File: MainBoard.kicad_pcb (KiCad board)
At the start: 2 copper layers, 120 x 68 mm, 89 parts, among them J1 DB25, P1 BOOT, P10 CONN_01X03, P11 CONN_01X03, P12 CONN_01X03, P13 CONN_01X03, P14 CONN_01X02, P15 CONN_02X07, P16 CONN_02X04, P18 CONN_01X03, P2 CONN_01X04, P3 CONN_02X04, P4 HOLE, P5 HOLE, P6 HOLE, P7 HOLE, P8 CONN_01X02, P9 CONN_01X03, Q1 BSS138, Q2 BSS138, Q3 DMN65D8L, SW1 RESET, U1 mp2307, U10 SI4425DDY, U11 INA199A2, U12 ADS1015, U2 DYS_mini_ESC, U3 DYS_mini_ESC, U4 DYS_mini_ESC, U5 DYS_mini_ESC, U6 TLV1117LV33, U7 TENDA_P200, U8 pca9685, U9 STM32F103CBT6, Y1 8MHz

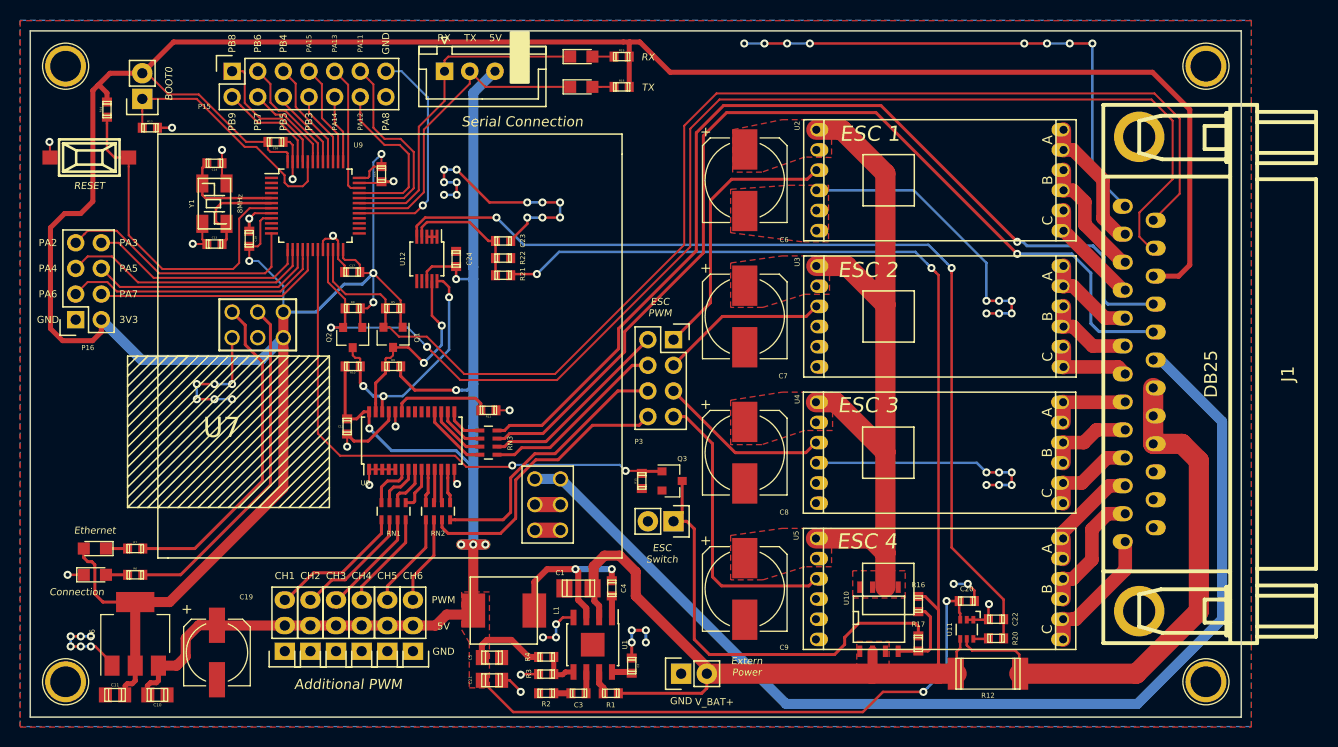
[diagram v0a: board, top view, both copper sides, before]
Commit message: replace groud via
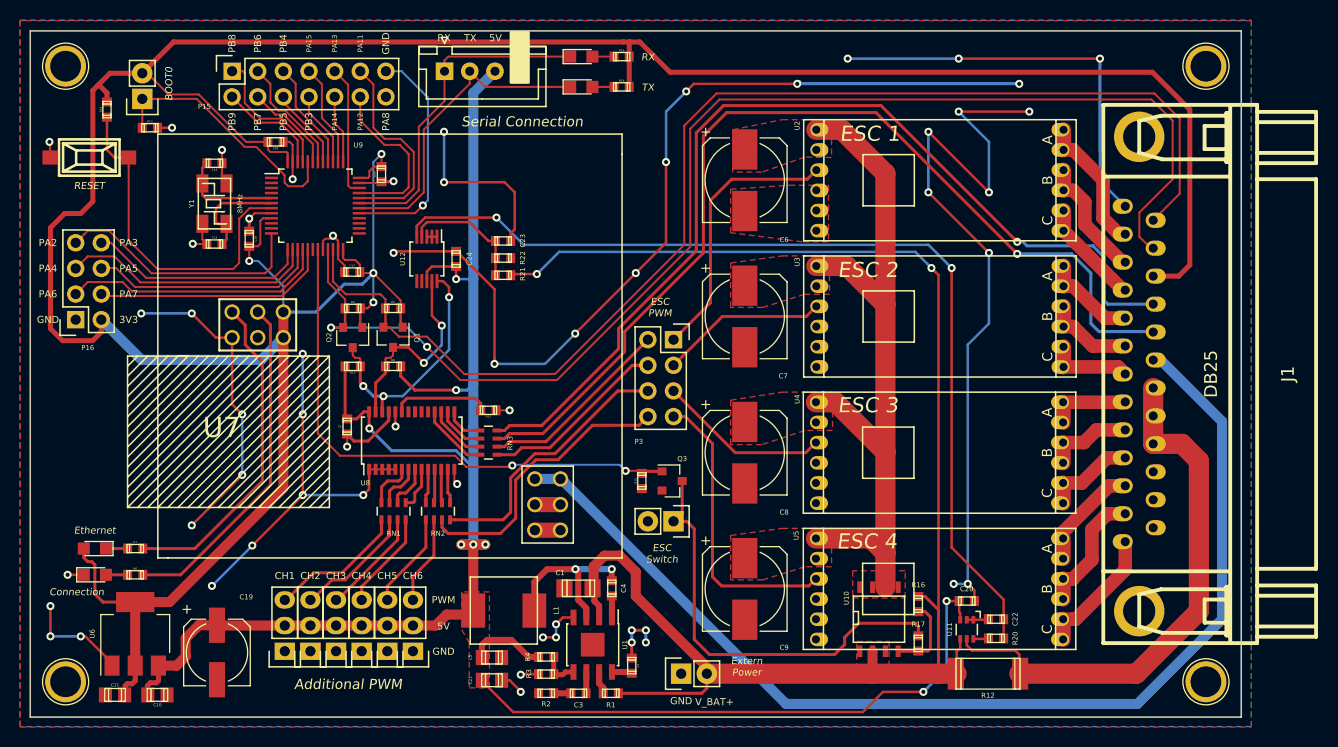
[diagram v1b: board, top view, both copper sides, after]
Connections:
- P4 pad 1: Net-(P4-Pad1) -> (no net)
- P5 pad 1: Net-(P5-Pad1) -> (no net)
- P6 pad 1: Net-(P6-Pad1) -> (no net)
- P7 pad 1: Net-(P7-Pad1) -> (no net)
- U12 pad 6: Net-(U12-Pad6) -> (no net)
- U12 pad 7: Net-(U12-Pad7) -> (no net)
- U7 pad P: Net-(U7-PadP) -> (no net)
- U8 pad 19: Net-(U8-Pad19) -> (no net)
- U8 pad 20: Net-(U8-Pad20) -> (no net)
- U8 pad 21: Net-(U8-Pad21) -> (no net)
- U8 pad 22: Net-(U8-Pad22) -> (no net)
- U9 pad 1: Net-(U9-Pad1) -> (no net)
- U9 pad 10: /PA0 -> (no net)
- U9 pad 11: /PA1 -> (no net)
- U9 pad 18: Net-(U9-Pad18) -> (no net)
- U9 pad 2: Net-(U9-Pad2) -> (no net)
- U9 pad 25: /PB12 -> (no net)
- U9 pad 26: /PB13 -> (no net)
- U9 pad 27: /PB14 -> (no net)
- U9 pad 28: /PB15 -> (no net)
- U9 pad 3: Net-(U9-Pad3) -> (no net)
- U9 pad 4: Net-(U9-Pad4) -> (no net)
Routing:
- net GND: track 227.5 -> 401.5 mm, vias 70 -> 57
